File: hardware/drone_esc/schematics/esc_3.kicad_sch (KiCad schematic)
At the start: 0 parts

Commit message: finished 4 esc schematics need further refinment of the sheets
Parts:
- added C31, C32, C33: 47uF 35V X7R MLCC, Capacitor_SMD:C_2220_5750Metric, symbol Device:C
- added C34, C35, C36: 10nF 10V X7R MLCC, Capacitor_SMD:C_0402_1005Metric, symbol Device:C
- added C37, C39, C40: 0.47uF 25V X7R MLCC, Capacitor_SMD:C_0603_1608Metric, symbol Device:C
- added C38: 4.7uF 25V X7R MLCC, Capacitor_SMD:C_1206_3216Metric, symbol Device:C
- added D7, D8, D9: BAT165, Drone_components:BAT165, symbol Drone_components:BAT165
- added Q13, Q14, Q15, Q16, Q17, Q18: BSC016N04LS, Drone_components:BSC016N04LS, symbol Drone_components:BSC016N04LS
- added R27, R28, R29, R30, R31, R32: 33, Resistor_SMD:R_0402_1005Metric, symbol Device:R
- added R33, R35, R37: 4.7k, Resistor_SMD:R_0402_1005Metric, symbol Device:R
- added R34, R36, R38: 1k, Resistor_SMD:R_0402_1005Metric, symbol Device:R
- added U7: FD6288Q, Drone_components:FD6288Q, symbol Drone_components:FD6288Q
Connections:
- new net: Q14.4, R28.2
- new net: C39.1, D8.1, U7.17 (VB2)
- new net: C40.1, D9.1, U7.14 (VB3)
- new net: Q18.4, R32.2
- new net: Q17.4, R31.2
- new net: Q16.4, R30.2
- new net: C37.1, D7.1, U7.20 (VB1)
- new net: Q15.4, R29.2
- new net: Q13.4, R27.2
- new net GND: C31.2, C32.2, C33.2, C34.2, C35.2, C36.2, C38.1, Q14.1-3, Q16.1-3, Q18.1-3, R34.1, R36.1, R38.1, U7.25 (EXP), U7.6 (COM)
- new net HIN3A: U7.22 (HIN1)
- new net HIN3B: U7.23 (HIN2)
- new net HIN3C: U7.24 (HIN3)
- new net HO1: R27.1, U7.19 (HO1)
- new net HO2: R29.1, U7.16 (HO2)
- new net HO3: R31.1, U7.13 (HO3)
- new net LIN3A: U7.1 (LIN1)
- new net LIN3B: U7.2 (LIN2)
- new net LIN3C: U7.3 (LIN3)
- new net LO1: R28.1, U7.11 (LO1)
- new net LO2: R30.1, U7.10 (LO2)
- new net LO3: R32.1, U7.9 (LO3)
- new net VCC: C31.1, C32.1, C33.1, C38.2, D7.2, D8.2, D9.2, Q13.5-8, Q15.5-8, Q17.5-8, U7.4 (VCC)
- new net VS1: C37.2, Q13.1-3, Q14.5-8, R33.2, U7.18 (VS1)
- new net VS2: C39.2, Q15.1-3, Q16.5-8, R35.2, U7.15 (VS2)
- new net VS3: C40.2, Q17.1-3, Q18.5-8, R37.2, U7.12 (VS3)
- new net VSense3A: C34.1, R33.1, R34.2
- new net VSense3B: C35.1, R35.1, R36.2
- new net VSense3C: C36.1, R37.1, R38.2

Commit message: finished the schematics and started to work on the PCB. need to find mcu model and finish the sheet description
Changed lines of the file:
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@@
 	(wire
 		(pts
-			(xy 78.74 50.8) (xy 78.74 44.45)
+			(xy 78.74 50.8) (xy 78.74 54.61)
 		)
 		(stroke
@@
 	(wire
 		(pts
+			(xy 78.74 44.45) (xy 78.74 50.8)
+		)
+		(stroke
+			(width 0)
+			(type default)
+		)
+	)
+	(wire
+		(pts
 			(xy 229.87 87.63) (xy 237.49 87.63)
 		)
@@
 	(wire
 		(pts
-			(xy 78.74 50.8) (xy 78.74 54.61)
-		)
-		(stroke
-			(width 0)
-			(type default)
-		)
-	)
-	(wire
-		(pts
 			(xy 78.74 158.75) (xy 105.41 158.75)
 		)
@@
 	)
 	(symbol
+		(lib_id "Drone_components:BSC016N04LS")
+		(at 78.74 39.37 0)
+		(unit 1)
+		(exclude_from_sim no)
+		(in_bom yes)
+		(on_board yes)
+		(dnp no)
+		(fields_autoplaced yes)
+		(property "Reference" "Q13"
+			(at 81.28 37.9964 0)
+			(effects
+				(font
+					(size 1.27 1.27)
+				)
+				(justify left)
+			)
+		)
+		(property "Value" "BSC016N04LS"
+			(at 81.28 40.5364 0)
+			(effects
+				(font
+					(size 1.27 1.27)
+				)
+				(justify left)
+			)
+		)
+		(property "Footprint" "Drone_components:BSC016N04LS"
+			(at 77.978 25.4 0)
+			(effects
+				(font
+					(size 1.27 1.27)
+				)
+				(justify bottom)
+				(hide yes)
+			)
+		)
+		(property "Datasheet" "https://www.lcsc.com/datasheet/C534294.pdf"
+			(at 78.74 39.37 0)
+			(effects
+				(font
+					(size 1.27 1.27)
+				)
+				(hide yes)
+			)
+		)
+		(property "Description" ""
+			(at 78.74 39.37 0)
+			(effects
+				(font
+					(size 1.27 1.27)
+				)
+				(hide yes)
+			)
+		)
+		(property "MF" "Infineon"
+			(at 78.74 14.478 0)
+			(effects
+				(font
+					(size 1.27 1.27)
+				)
+				(justify bottom)
+				(hide yes)
+			)
+		)
+		(property "Description_1" "N-Channel 40 V 31A (Ta), 100A (Tc) 2.5W (Ta), 139W (Tc) Surface Mount PG-TDSON-8-1"
+			(at 78.74 27.94 0)
+			(effects
+				(font
+					(size 1.27 1.27)
+				)
+				(justify bottom)
+				(hide yes)
+			)
+		)
+		(property "Package" "None"
+			(at 78.74 23.876 0)
+			(effects
+				(font
+					(size 1.27 1.27)
+				)
+				(justify bottom)
+				(hide yes)
+			)
+		)
+		(property "Price" "None"
+			(at 78.74 39.37 0)
+			(effects
+				(font
+					(size 1.27 1.27)
+				)
+				(justify bottom)
+				(hide yes)
+			)
+		)
+		(property "SnapEDA_Link" "https://www.snapeda.com/parts/BSC016N04LS/Infineon/view-part/?ref=snap"
+			(at 78.994 22.352 0)
+			(effects
+				(font
+					(size 1.27 1.27)
+				)
+				(justify bottom)
+				(hide yes)
+			)
+		)
+		(property "MP" "BSC016N04LS"
+			(at 78.232 17.018 0)
+			(effects
+				(font
+					(size 1.27 1.27)
+				)
+				(justify bottom)
+				(hide yes)
+			)
+		)
+		(property "Availability" "In Stock"
+			(at 78.74 12.446 0)
+			(effects
+				(font
+					(size 1.27 1.27)
+				)
+				(justify bottom)
+				(hide yes)
+			)
+		)
+		(property "Check_prices" "https://www.snapeda.com/parts/BSC016N04LS/Infineon/view-part/?ref=eda"
+			(at 77.978 19.558 0)
+			(effects
+				(font
+					(size 1.27 1.27)
+				)
+				(justify bottom)
+				(hide yes)
+			)
+		)
+		(property "JLCPCB part" "C534294"
+			(at 78.74 39.37 0)
+			(effects
+				(font
+					(size 1.27 1.27)
+				)
+				(hide yes)
+			)
+		)
+		(pin "1-3"
+		)
+		(pin "4"
+		)
+		(pin "5-8"
+		)
+		(instances
+			(project "drone_esc"
+				(path "/b5a13fd4-6868-4fff-a56c-eae40f1d53c7/197a88c0-01e6-4a4c-9363-f93dfbc08269"
+					(reference "Q13")
+					(unit 1)
+				)
+			)
+		)
+	)
+	(symbol
 		(lib_id "Device:C")
 		(at 119.38 173.99 0)
@@
 					(unit 1)
 				)
-			)
-		)
-	)
-	(symbol
-		(lib_id "Drone_components:BSC016N04LS")
-		(at 78.74 39.37 0)
-		(unit 1)
-		(exclude_from_sim no)
-		(in_bom yes)
-		(on_board yes)
-		(dnp no)
-		(fields_autoplaced yes)
-		(property "Reference" "Q13"
-			(at 81.28 37.9964 0)
-			(effects
-				(font
-					(size 1.27 1.27)
-				)
-				(justify left)
-			)
-		)
-		(property "Value" "BSC016N04LS"
-			(at 81.28 40.5364 0)
-			(effects
-				(font
-					(size 1.27 1.27)
-				)
-				(justify left)
-			)
-		)
-		(property "Footprint" "Drone_components:BSC016N04LS"
-			(at 77.978 25.4 0)
-			(effects
-				(font
-					(size 1.27 1.27)
-				)
-				(justify bottom)
-				(hide yes)
-			)
-		)
-		(property "Datasheet" "https://www.lcsc.com/datasheet/C534294.pdf"
-			(at 78.74 39.37 0)
-			(effects
-				(font
-					(size 1.27 1.27)
-				)
-				(hide yes)
-			)
-		)
-		(property "Description" ""
-			(at 78.74 39.37 0)
-			(effects
-				(font
-					(size 1.27 1.27)
-				)
-				(hide yes)
-			)
-		)
-		(property "MF" "Infineon"
-			(at 78.74 14.478 0)
-			(effects
-				(font
-					(size 1.27 1.27)
-				)
-				(justify bottom)
-				(hide yes)
-			)
-		)
-		(property "Description_1" "N-Channel 40 V 31A (Ta), 100A (Tc) 2.5W (Ta), 139W (Tc) Surface Mount PG-TDSON-8-1"
-			(at 78.74 27.94 0)
-			(effects
-				(font
-					(size 1.27 1.27)
-				)
-				(justify bottom)
-				(hide yes)
-			)
-		)
-		(property "Package" "None"
-			(at 78.74 23.876 0)
-			(effects
-				(font
-					(size 1.27 1.27)
-				)
-				(justify bottom)
-				(hide yes)
-			)
-		)
-		(property "Price" "None"
-			(at 78.74 39.37 0)
-			(effects
-				(font
-					(size 1.27 1.27)
-				)
-				(justify bottom)
-				(hide yes)
-			)
-		)
-		(property "SnapEDA_Link" "https://www.snapeda.com/parts/BSC016N04LS/Infineon/view-part/?ref=snap"
-			(at 78.994 22.352 0)
-			(effects
-				(font
-					(size 1.27 1.27)
-				)
-				(justify bottom)
-				(hide yes)
-			)
-		)
-		(property "MP" "BSC016N04LS"
-			(at 78.232 17.018 0)
-			(effects
-				(font
-					(size 1.27 1.27)
-				)
-				(justify bottom)
-				(hide yes)
-			)
-		)
-		(property "Availability" "In Stock"
-			(at 78.74 12.446 0)
-			(effects
-				(font
-					(size 1.27 1.27)
-				)
-				(justify bottom)
-				(hide yes)
-			)
-		)
-		(property "Check_prices" "https://www.snapeda.com/parts/BSC016N04LS/Infineon/view-part/?ref=eda"
-			(at 77.978 19.558 0)
-			(effects
-				(font
-					(size 1.27 1.27)
-				)
-				(justify bottom)
-				(hide yes)
-			)
-		)
-		(property "JLCPCB part" "C534294"
-			(at 78.74 39.37 0)
-			(effects
-				(font
-					(size 1.27 1.27)
-				)
-				(hide yes)
-			)
-		)
-		(pin "1-3"
-		)
-		(pin "4"
-		)
-		(pin "5-8"
-		)
-		(instances
-			(project "drone_esc"
-				(path "/b5a13fd4-6868-4fff-a56c-eae40f1d53c7/197a88c0-01e6-4a4c-9363-f93dfbc08269"
-					(reference "Q13")
-					(unit 1)
-				)

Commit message: continued developing the pcb board
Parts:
- C31, C32, C33: value 47uF 35V X7R MLCC -> 22uF 25V X5R MLCC; footprint Capacitor_SMD:C_2220_5750Metric -> Capacitor_SMD:C_1210_3225Metric; JLCPCB part C3873016 -> C12891
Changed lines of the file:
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@@
+	)
+	(symbol
+		(lib_id "Device:C")
+		(at 104.14 34.29 0)
+		(unit 1)
+		(exclude_from_sim no)
+		(in_bom yes)
+		(on_board yes)
+		(dnp no)
+		(fields_autoplaced yes)
+		(property "Reference" "C31"
+			(at 107.95 33.0199 0)
+			(effects
+				(font
+					(size 1.27 1.27)
+				)
+				(justify left)
+			)
+		)
+		(property "Value" "22uF 25V X5R MLCC"
+			(at 107.95 35.5599 0)
+			(effects
+				(font
+					(size 1.27 1.27)
+				)
+				(justify left)
+			)
+		)
+		(property "Footprint" "Capacitor_SMD:C_1210_3225Metric"
+			(at 105.1052 38.1 0)
+			(effects
+				(font
+					(size 1.27 1.27)
+				)
+				(hide yes)
+			)
+		)
+		(property "Datasheet" "~"
+			(at 104.14 34.29 0)
+			(effects
+				(font
+					(size 1.27 1.27)
+				)
+				(hide yes)
+			)
+		)
+		(property "Description" "Unpolarized capacitor"
+			(at 104.14 34.29 0)
+			(effects
+				(font
+					(size 1.27 1.27)
+				)
+				(hide yes)
+			)
+		)
+		(property "JLCPCB part" "C12891"
+			(at 104.14 34.29 0)
+			(effects
+				(font
+					(size 1.27 1.27)
+				)
+				(hide yes)
+			)
+		)
+		(pin "2"
+		)
+		(pin "1"
+		)
+		(instances
+			(project "drone_esc"
+				(path "/b5a13fd4-6868-4fff-a56c-eae40f1d53c7/197a88c0-01e6-4a4c-9363-f93dfbc08269"
+					(reference "C31")
+					(unit 1)
+				)
+			)
+		)
 	)
 	(symbol
@@
 	)
 	(symbol
-		(lib_id "Device:C")
-		(at 104.14 34.29 0)
-		(unit 1)
-		(exclude_from_sim no)
-		(in_bom yes)
-		(on_board yes)
-		(dnp no)
-		(fields_autoplaced yes)
-		(property "Reference" "C31"
-			(at 107.95 33.0199 0)
-			(effects
-				(font
-					(size 1.27 1.27)
-				)
-				(justify left)
-			)
-		)
-		(property "Value" "47uF 35V X7R MLCC"
-			(at 107.95 35.5599 0)
-			(effects
-				(font
-					(size 1.27 1.27)
-				)
-				(justify left)
-			)
-		)
-		(property "Footprint" "Capacitor_SMD:C_2220_5750Metric"
-			(at 105.1052 38.1 0)
+		(lib_id "Device:R")
+		(at 105.41 173.99 180)
+		(unit 1)
+		(exclude_from_sim no)
+		(in_bom yes)
+		(on_board yes)
+		(dnp no)
+		(property "Reference" "R38"
+			(at 108.458 172.974 0)
+			(effects
+				(font
+					(size 1.27 1.27)
+				)
+			)
+		)
+		(property "Value" "1k"
+			(at 108.458 175.006 0)
+			(effects
+				(font
+					(size 1.27 1.27)
+				)
+			)
+		)
+		(property "Footprint" "Resistor_SMD:R_0402_1005Metric"
+			(at 107.188 173.99 90)
 			(effects
 				(font
@@
 		)
 		(property "Datasheet" "~"
-			(at 104.14 34.29 0)
-			(effects
-				(font
-					(size 1.27 1.27)
-				)
-				(hide yes)
-			)
-		)
-		(property "Description" "Unpolarized capacitor"
-			(at 104.14 34.29 0)
-			(effects
-				(font
-					(size 1.27 1.27)
-				)
-				(hide yes)
-			)
-		)
-		(property "JLCPCB part" "C3873016"
-			(at 104.14 34.29 0)
-			(effects
-				(font
-					(size 1.27 1.27)
-				)
-				(hide yes)
-			)
+			(at 105.41 173.99 0)
+			(effects
+				(font
+					(size 1.27 1.27)
+				)
+				(hide yes)
+			)
+		)
+		(property "Description" "Resistor"
+			(at 105.41 173.99 0)
+			(effects
+				(font
+					(size 1.27 1.27)
+				)
+				(hide yes)
+			)
+		)
+		(property "JLCPCB part" "C11702"
+			(at 105.41 173.99 0)
+			(effects
+				(font
+					(size 1.27 1.27)
+				)
+				(hide yes)
+			)
+		)
+		(pin "1"
 		)
 		(pin "2"
 		)
-		(pin "1"
-		)
-		(instances
-			(project "drone_esc"
-				(path "/b5a13fd4-6868-4fff-a56c-eae40f1d53c7/197a88c0-01e6-4a4c-9363-f93dfbc08269"
-					(reference "C31")
+		(instances
+			(project "drone_esc"
+				(path "/b5a13fd4-6868-4fff-a56c-eae40f1d53c7/197a88c0-01e6-4a4c-9363-f93dfbc08269"
+					(reference "R38")
 					(unit 1)
 				)
@@
 			)
 		)
-		(property "Value" "47uF 35V X7R MLCC"
+		(property "Value" "22uF 25V X5R MLCC"
 			(at 107.95 88.8999 0)
 			(effects
@@
 			)
 		)
-		(property "Footprint" "Capacitor_SMD:C_2220_5750Metric"
+		(property "Footprint" "Capacitor_SMD:C_1210_3225Metric"
 			(at 105.1052 91.44 0)
 			(effects
@@
 			)
 		)
-		(property "JLCPCB part" "C3873016"
+		(property "JLCPCB part" "C12891"
 			(at 104.14 87.63 0)
 			(effects
@@
 				(path "/b5a13fd4-6868-4fff-a56c-eae40f1d53c7/197a88c0-01e6-4a4c-9363-f93dfbc08269"
 					(reference "C32")
-					(unit 1)
-				)
-			)
-		)
-	)
-	(symbol
-		(lib_id "Device:R")
-		(at 105.41 173.99 180)
-		(unit 1)
-		(exclude_from_sim no)
-		(in_bom yes)
-		(on_board yes)
-		(dnp no)
-		(property "Reference" "R38"
-			(at 108.458 172.974 0)
-			(effects
-				(font
-					(size 1.27 1.27)
-				)
-			)
-		)
-		(property "Value" "1k"
-			(at 108.458 175.006 0)
-			(effects
-				(font
-					(size 1.27 1.27)
-				)
-			)
-		)
-		(property "Footprint" "Resistor_SMD:R_0402_1005Metric"
-			(at 107.188 173.99 90)
-			(effects
-				(font
-					(size 1.27 1.27)
-				)
-				(hide yes)
-			)
-		)
-		(property "Datasheet" "~"
-			(at 105.41 173.99 0)
-			(effects
-				(font
-					(size 1.27 1.27)
-				)
-				(hide yes)
-			)
-		)
-		(property "Description" "Resistor"
-			(at 105.41 173.99 0)
-			(effects
-				(font
-					(size 1.27 1.27)
-				)
-				(hide yes)
-			)
-		)
-		(property "JLCPCB part" "C11702"
-			(at 105.41 173.99 0)
-			(effects
-				(font
-					(size 1.27 1.27)
-				)
-				(hide yes)
-			)
-		)
-		(pin "1"
-		)
-		(pin "2"
-		)
-		(instances
-			(project "drone_esc"
-				(path "/b5a13fd4-6868-4fff-a56c-eae40f1d53c7/197a88c0-01e6-4a4c-9363-f93dfbc08269"
-					(reference "R38")
 					(unit 1)
 				)
@@
 			)
 		)
-		(property "Value" "47uF 35V X7R MLCC"
+		(property "Value" "22uF 25V X5R MLCC"
 			(at 107.95 143.5099 0)
 			(effects
@@
 			)
 		)
-		(property "Footprint" "Capacitor_SMD:C_2220_5750Metric"
+		(property "Footprint" "Capacitor_SMD:C_1210_3225Metric"
 			(at 105.1052 146.05 0)
 			(effects
@@
 			)
 		)
-		(property "JLCPCB part" "C3873016"
+		(property "JLCPCB part" "C12891"
 			(at 104.14 142.24 0)
 			(effects

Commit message: finnished component placement
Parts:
- removed D7, D8, D9: BAT165, Drone_components:BAT165, symbol Drone_components:BAT165
- added D7, D8, D9: RB520S30, Drone_components:RB520S30, symbol Drone_components:RB520S30
- C37, C39, C40: value 0.47uF 25V X7R MLCC -> 1uF 25V X5R MLCC; footprint Capacitor_SMD:C_0603_1608Metric -> Capacitor_SMD:C_0402_1005Metric; JLCPCB part C1623 -> C52923
- C38: value 4.7uF 25V X7R MLCC -> 10uF 25V X5R MLCC; footprint Capacitor_SMD:C_1206_3216Metric -> Capacitor_SMD:C_0603_1608Metric; JLCPCB part C29823 -> C96446
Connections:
- net VCC: now also D7.2, D8.2, D9.2
- net at C39.1, U7.17 (VB2): now also D8.1
- net at C40.1, U7.14 (VB3): now also D9.1
- net at C37.1, U7.20 (VB1): now also D7.1

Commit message: replaced some of the schematics
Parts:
- removed Q13, Q14, Q15, Q16, Q17, Q18: BSC016N04LS, Drone_components:BSC016N04LS, symbol Drone_components:BSC016N04LS
- added Q13, Q14, Q15, Q16, Q17, Q18: BSC009NE2LS5IATMA1, Drone_components:BSC093N04LSGATMA1, symbol Drone_components:BSC009NE2LS5IATMA1
- C31, C32, C33: footprint Capacitor_SMD:C_1210_3225Metric -> Capacitor_SMD:C_0805_2012Metric; JLCPCB part C12891 -> C45783
- R27, R28, R29, R30, R31, R32: value 33 -> 47
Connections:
- net GND: now also Q14.1, Q14.2, Q14.3, Q16.1, Q16.2, Q16.3, Q18.1, Q18.2, Q18.3
- net VCC: now also Q13.5, Q15.5, Q17.5
- net VS1: now also Q13.1, Q13.2, Q13.3, Q14.5
- net VS2: now also Q15.1, Q15.2, Q15.3, Q16.5
- net VS3: now also Q17.1, Q17.2, Q17.3, Q18.5
- net at R28.2: now also Q14.4
- net at R32.2: now also Q18.4
- net at R31.2: now also Q17.4
- net at R30.2: now also Q16.4
- net at R27.2: now also Q13.4
- net at R29.2: now also Q15.4
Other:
- moved on the sheet: R27, R28, R29, R30, R31, R32

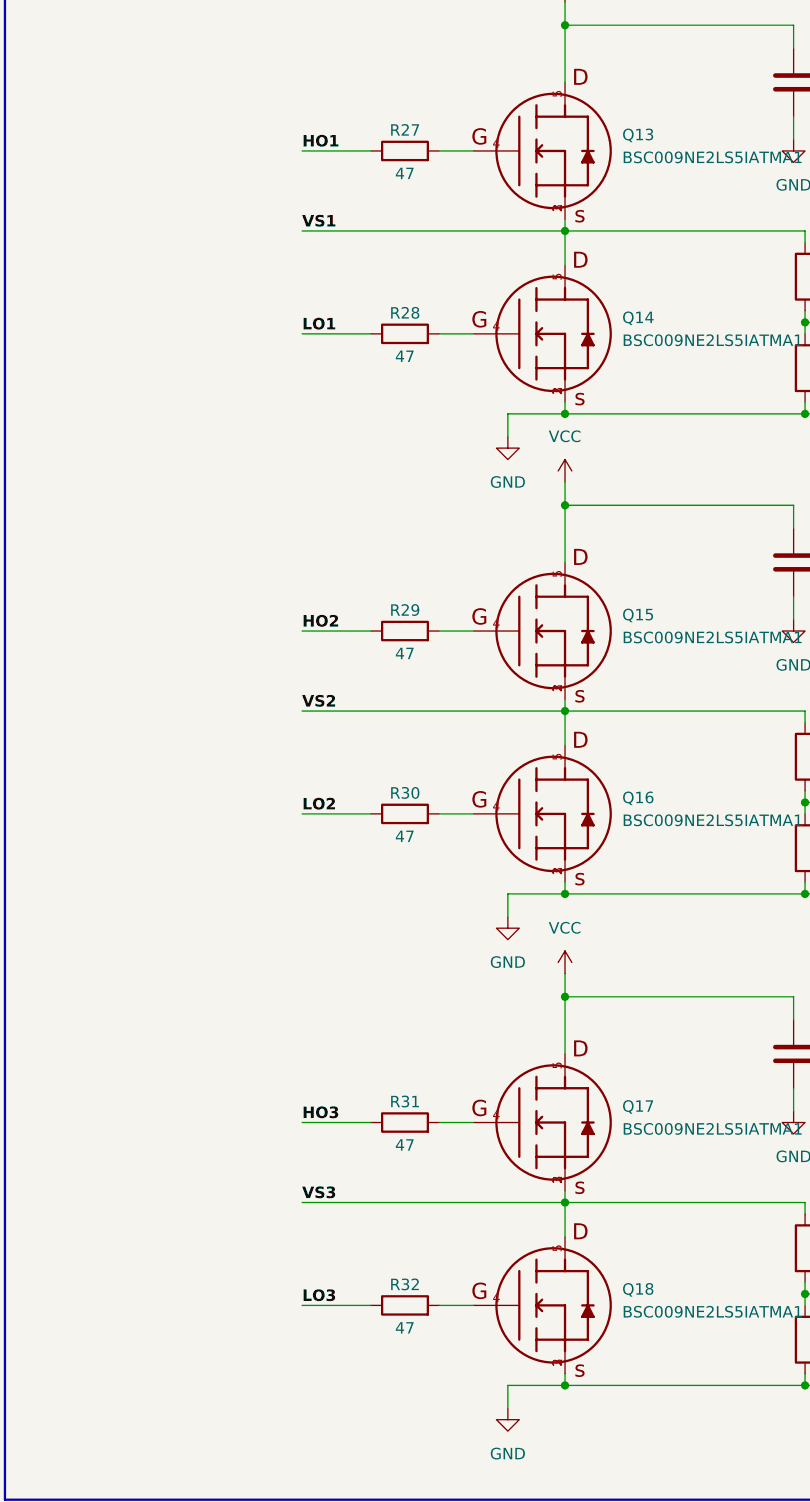
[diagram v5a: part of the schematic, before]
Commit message: changed some footprints and reconstracted the latout with better gate resistors clearence
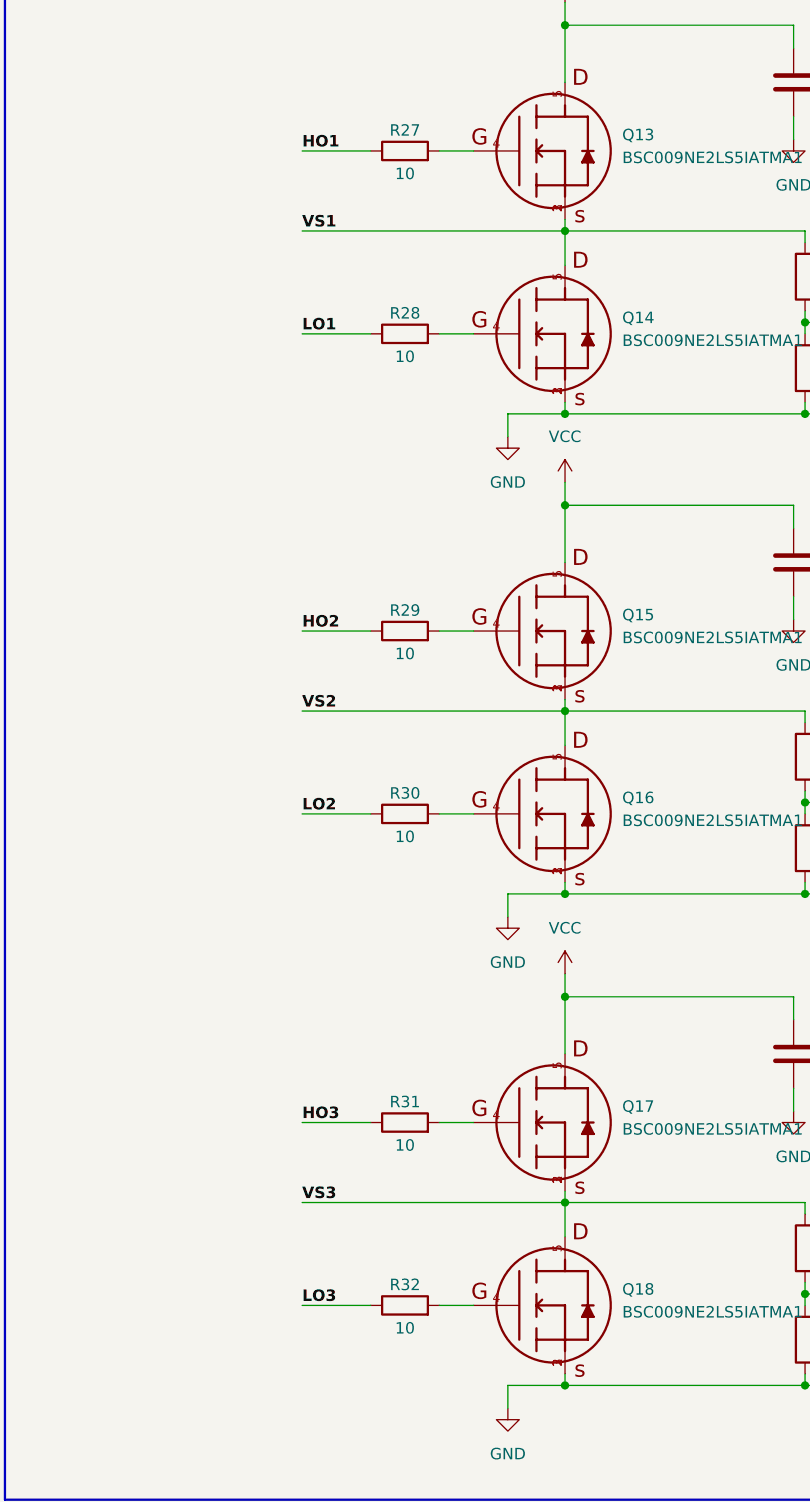
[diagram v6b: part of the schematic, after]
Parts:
- R27, R28, R29, R30, R31, R32: value 47 -> 10; footprint Resistor_SMD:R_0402_1005Metric -> Resistor_SMD:R_0201_0603Metric; JLCPCB part C25105 -> C105889
